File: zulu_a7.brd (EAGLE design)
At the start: 61 x 25.4 mm, 169 parts, among them J1 Pmod 2x6, Q1 12MHz 25ppm (FPGA + FT2232HQ), Q3 MBT3904DW1T1, U1 XC7A35T-1CPG236C, U10 93LC46BT-I/SN, U2 FT2232HQ USB-UART/JTAG Bridge, U3 AS4C32M16SB-6TIN, U4 W25Q128JVSIQ, U8 LTC3569EUDC#TRPBF, X1 Molex 105017-0001 Micro-USB-B

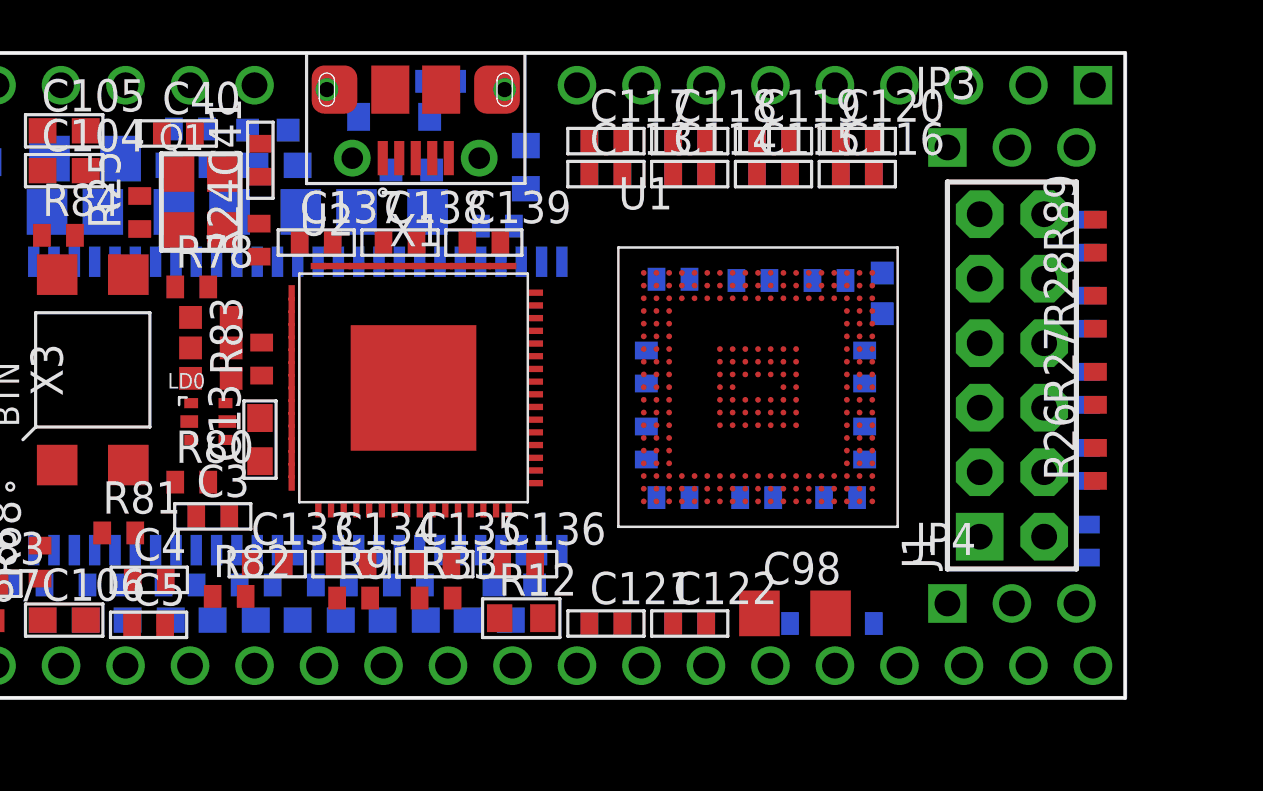
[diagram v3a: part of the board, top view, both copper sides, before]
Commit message: The eight Pmod series resistors go 0402 -> 0201
R26-R33, the 200R in series with the Pmod's eight signal pins. New R0201
package in rcl and an R0201 device on R-US_SMALL; the parts keep their value,
their nets and their 1 % tolerance.

WHAT IT BOUGHT. All eight now sit in a 2x4 block at x 59.49 and 60.09, y 8.60
to 13.99, hard against J1 -- which is where a series resistor for a connector
pin belongs. R33 came off the hand-pin it needed two commits ago: at 0402 it
would not seat within 24 mm of J1 and had to be stranded at x 33; at 0201 the
anchored pass reaches it and it rejoined its seven siblings. Keepout per part
falls 2.95 x 0.97 to 1.75 x 0.37, about a quarter of the area.

THE POWER RATING IS THE THING TO KNOW. These resistors exist for one case: a
Pmod pin driven high into a short. That is 3.3 V across 200 R = 16.5 mA and
54.4 mW, sustained. An 0402 at 1/16 W has 62.5 mW and takes it at 87 %. An 0201
at 1/20 W has 50 mW and is at 109 % -- over rating, not under. It is a fault
case and not normal operation, and Cmod A7 evidently accepts the same, so this
follows that lead. But the margin that existed is gone, and a resistor that
cooks in the fault it was put there to survive is worth knowing about.

The land pattern is marked PROVISIONAL in the package, the way ESP-11 is. It is
0.30 x 0.30 pads on a 0.20 gap, a conventional 0201 land -- deliberately NOT
scaled from R0402 here, which carries a 0.50 mm toe that is generous for hand
work and would pull 0201 parts into tombstones. Check it against the maker's
recommendation and the assembler's 0201 capability before fabricating; 0201 is
not reworkable by hand.

Caught while doing it: the SPEC string "thick film +-1%, 1/16W, 0402" is shared
by 50 parts, so a blind replace relabelled 42 still-0402 resistors as 0201.
Every part's device and SPEC now agree, and the only R-parts without a SPEC are
the six that never had one.

157 placed, 8 real parts parked, unchanged. check_board and validate 0 findings.

Co-Authored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
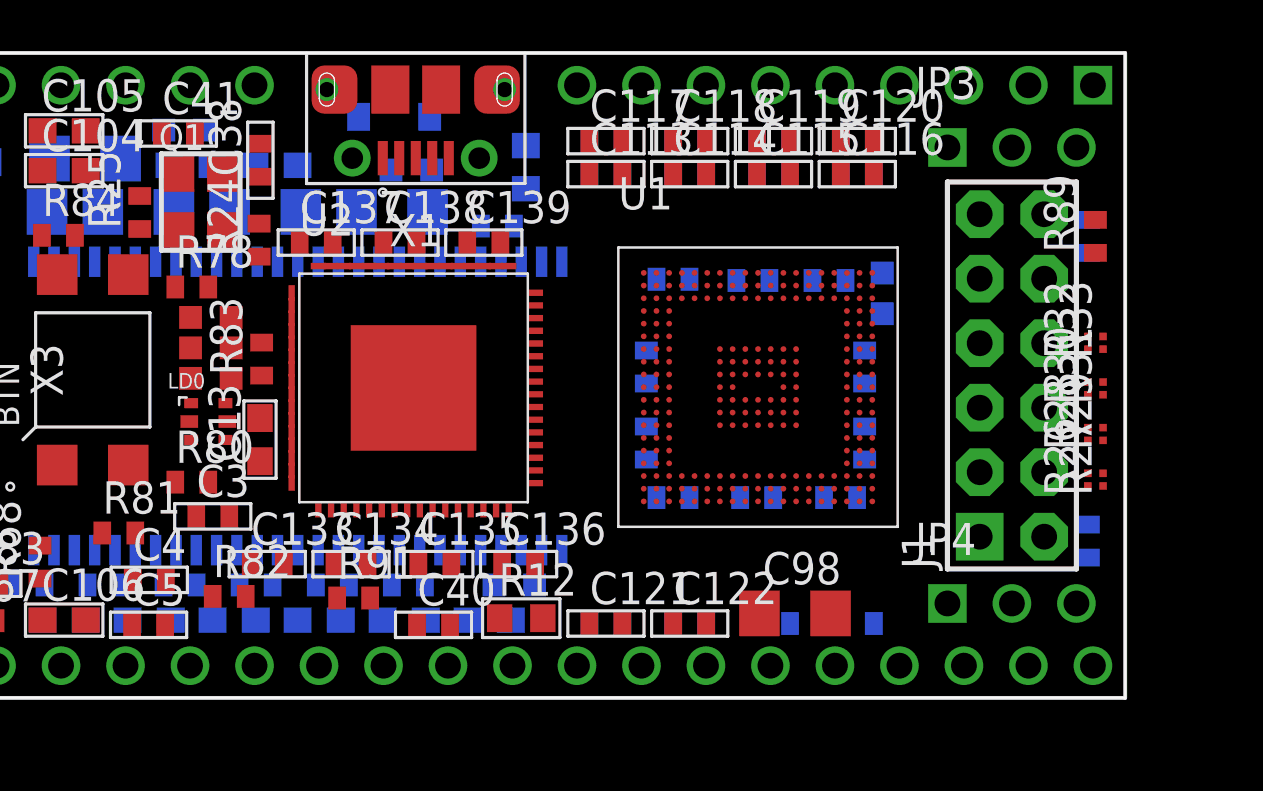
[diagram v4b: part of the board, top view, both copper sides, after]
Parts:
- R26, R27, R28, R29, R30, R31, R32, R33: device rcl:R0402 -> rcl:R0201
- moved R33 28.1 mm to (60.1, 14.0), turned to 90 degrees
- moved R32 27.5 mm to (59.5, 14.0), flipped to the top, turned to 90 degrees
- moved C40 21.8 mm to (33.7, 2.88)
- moved R28 4.81 mm to (59.5, 10.4)
- moved R27 3.61 mm to (60.1, 8.60)
- moved C41 3.40 mm to (23.7, 22.2), turned to 0 degrees
- moved L5 3.30 mm to (23.9, 22.4)
- moved R31 3.06 mm to (60.1, 12.2), flipped to the top
- moved C38 3.02 mm to (26.9, 21.2), flipped to the top, turned to 90 degrees
- moved R29 1.33 mm to (60.1, 10.4), flipped to the top
- moved R26 0.67 mm to (59.5, 8.60)
- flipped R30 to the top
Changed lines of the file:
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@@
 <element name="C137" library="rcl" package="C0402" value="0.1uF" x="29.1" y="17.933"/>
 <element name="C138" library="rcl" package="C0402" value="0.1uF" x="32.4" y="17.933"/>
-<element name="R26" library="rcl" package="R0402" value="200" x="59.79" y="9.198" rot="R90"/>
-<element name="R27" library="rcl" package="R0402" value="200" x="59.79" y="12.194" rot="R90"/>
-<element name="R28" library="rcl" package="R0402" value="200" x="59.79" y="15.19" rot="R90"/>
-<element name="R29" library="rcl" package="R0402" value="200" x="59.5098" y="9.198" rot="MR90"/>
-<element name="R30" library="rcl" package="R0402" value="200" x="59.5098" y="12.194" rot="MR90"/>
-<element name="R31" library="rcl" package="R0402" value="200" x="59.5098" y="15.19" rot="MR90"/>
-<element name="R32" library="rcl" package="R0402" value="200" x="33.998" y="24.284" rot="MR0"/>
-<element name="R33" library="rcl" package="R0402" value="200" x="33.823" y="3.933"/>
+<element name="R26" library="rcl" package="R0201" value="200" x="59.49" y="8.598" rot="R90"/>
+<element name="R27" library="rcl" package="R0201" value="200" x="60.09" y="8.598" rot="R90"/>
+<element name="R28" library="rcl" package="R0201" value="200" x="59.49" y="10.394" rot="R90"/>
+<element name="R29" library="rcl" package="R0201" value="200" x="60.09" y="10.394" rot="R90"/>
+<element name="R30" library="rcl" package="R0201" value="200" x="59.49" y="12.19" rot="R90"/>
+<element name="R31" library="rcl" package="R0201" value="200" x="60.09" y="12.19" rot="R90"/>
+<element name="R32" library="rcl" package="R0201" value="200" x="59.49" y="13.986" rot="R90"/>
+<element name="R33" library="rcl" package="R0201" value="200" x="60.09" y="13.986" rot="R90"/>
 <element name="U$2" library="ctambe" package="CC_CC" value="" x="5.0585" y="-6.4415"/>
 <element name="U$3" library="ctambe" package="CC_BY" value="" x="10.895" y="-7.722"/>
@@
 <element name="L3" library="ctambe" package="IND2520" value="2.2uH" x="12.45" y="16.34" rot="MR0"/>
 <element name="L4" library="ctambe" package="IND0603" value="FB 600R@100MHz" x="32.845" y="20.79" rot="MR0"/>
-<element name="L5" library="ctambe" package="IND0603" value="FB 600R@100MHz" x="27.196" y="22.36" rot="MR0"/>
+<element name="L5" library="ctambe" package="IND0603" value="FB 600R@100MHz" x="23.896" y="22.36" rot="MR0"/>
 <element name="L6" library="ctambe" package="IND0603" value="FB 600R@100MHz" x="51.392" y="15.932" rot="MR90"/>
 <element name="L7" library="ctambe" package="IND0603" value="FB 600R@100MHz" x="36.9" y="4.45" rot="MR0"/>
@@
 <element name="C139" library="rcl" package="C0402" value="3.3uF" x="35.7" y="17.933"/>
 <element name="C39" library="rcl" package="C0402" value="3.3uF" x="36.234" y="18.58" rot="MR0"/>
-<element name="C40" library="rcl" package="C0402" value="100nF" x="23.6705" y="22.23"/>
-<element name="C41" library="rcl" package="C0402" value="100nF" x="26.9" y="21.176" rot="R90"/>
+<element name="C40" library="rcl" package="C0402" value="100nF" x="33.721" y="2.878"/>
+<element name="C41" library="rcl" package="C0402" value="100nF" x="23.6705" y="22.23"/>
 <element name="R71" library="rcl" package="R0402" value="180K 1%" x="6.169" y="2.828" rot="MR0"/>
 <element name="C83" library="rcl" package="C0402" value="20pF" x="15.973" y="4.5"/>
@@
 <element name="R85" library="rcl" package="R0402" value="10K" x="15.65" y="13.364" rot="MR90"/>
 <element name="R86" library="rcl" package="R0402" value="10K" x="15.65" y="16.36" rot="MR90"/>
-<element name="R89" library="rcl" package="R0402" value="10K" x="59.79" y="18.186" rot="R90"/>
+<element name="R89" library="rcl" package="R0402" value="10K" x="59.79" y="18.178" rot="R90"/>
 <element name="R90" library="rcl" package="R0402" value="10K" x="59.5098" y="6.176" rot="MR90"/>
 <element name="R91" library="rcl" package="R0402" value="10K" x="30.573" y="3.933"/>
-<element name="R92" library="rcl" package="R0402" value="10K" x="59.5098" y="18.186" rot="MR90"/>
+<element name="R92" library="rcl" package="R0402" value="10K" x="59.5098" y="18.178" rot="MR90"/>
 <element name="R93" library="rcl" package="R0402" value="10K" x="42.1" y="13.034" rot="MR90"/>
 <element name="R94" library="rcl" package="R0402" value="10K" x="50.7" y="13.034" rot="MR90"/>
@@
 <element name="BTN" library="ctambe" package="PTA-142" value="PTA-142" x="20.3" y="12.92" rot="R90"/>
 <element name="Q1" library="ctambe" package="32X25" value="12MHz 25ppm (FPGA + FT2232HQ)" x="23.7" y="20.63"/>
-<element name="C38" library="rcl" package="C0402" value="0.01uF" x="24.146" y="22.41" rot="MR0"/>
+<element name="C38" library="rcl" package="C0402" value="0.01uF" x="26.9" y="21.176" rot="R90"/>
 <element name="J1" library="ctambe" package="2X06" value="Pmod 2x6" x="56.5" y="12.7" rot="R90"/>
 <element name="R24" library="rcl" package="R0402" value="33" x="26.85" y="18.028" rot="R90"/>

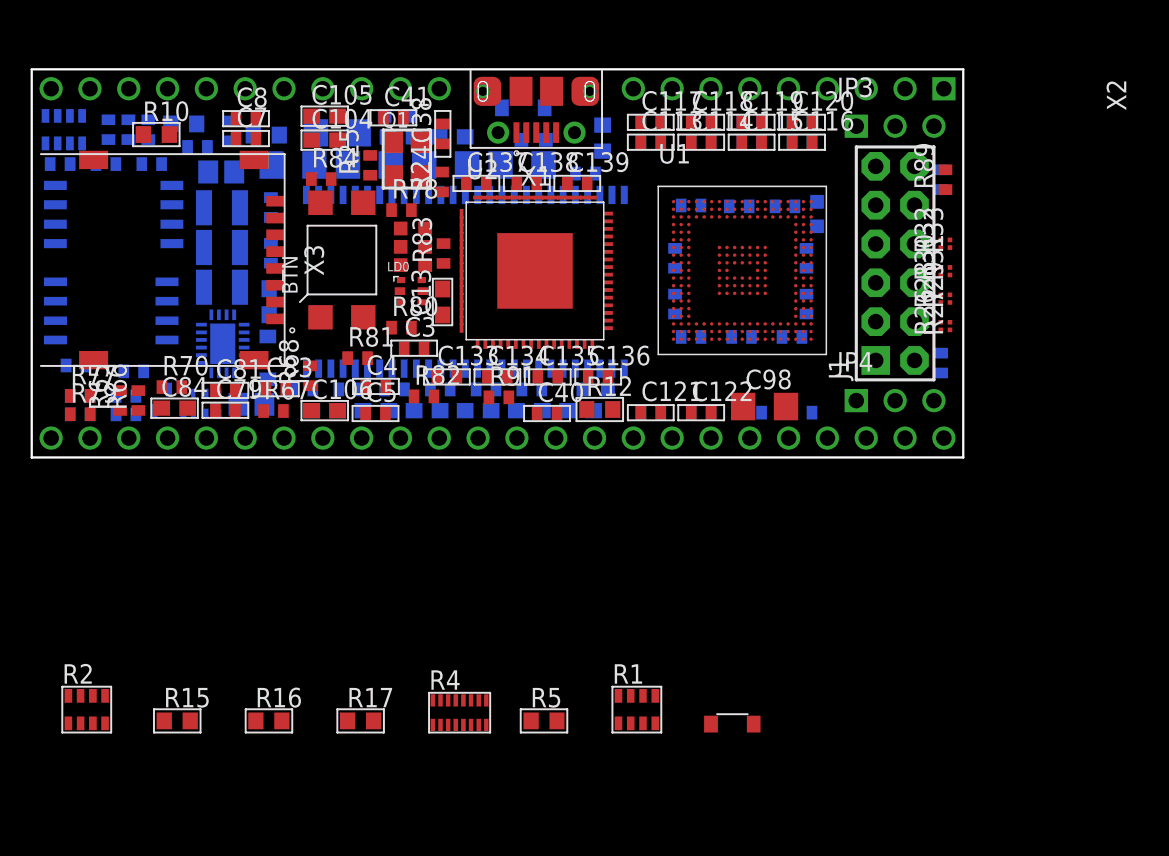
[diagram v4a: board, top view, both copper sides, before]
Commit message: The eight XADC resistors go 0603 -> 0201, and five parts come off the park
R10-R17, both XADC channels: the 2.32k/1k divider, the 140R into AIN_P and the
845R from AIN_N to ground. R-US_ gains an R0201 device; values, nets and 1 %
tolerance unchanged.

POWER IS NOT THE QUESTION HERE, unlike the Pmod eight. The only ones carrying
current are R10/R14 at the top of a 3.32k divider: 2.3 mW at a 3.3 V input,
5.3 mW at 5 V, against an 0201's 50 mW. Eleven per cent of rating at the worst
case, nine times the margin. R12/R13/R16/R17 sit on XADC inputs and carry
leakage. Nothing here cooks the way a shorted Pmod pin does.

Nor does size touch what this circuit depends on. R13 = 845R is matching
R12 + (R10||R11) = 838.8R so both XADC inputs see the same source impedance,
and that is a tolerance property. 1 % is 1 % at any size.

WHAT IT FREED. Parked real parts 8 -> 3. R15, R16 and R17 seated, and the space
released also let D3 and R5 in. The four that matter most are close: R12 5.6 mm
from the ball centre, R17 5.5, R16 6.2, R13 7.2 -- the network at the XADC pins
is tight to the package. R10/R11 and R14/R15 landed 20 to 24 mm out, which is
fine for a divider that only scales the input before it reaches that network.

WHAT IS LEFT: R1, R2 and R4, all three array packages, which no amount of chip
shrinking helps. Splitting them into 16 discrete 0402 is still the open option.

AND ONE THING TO LOOK AT. D3 is on the board now, at 51.3 mm from X2 pad 1. I
had left it parked on purpose because 55 mm from the pin a TVS protects is not
protection. Freeing space did not fix that -- it just let the anchored pass seat
it, at the far end, where it clamps no better than it did unplaced. It now looks
placed. It is not placed usefully, and dropping JP3/JP4 is still what would give
it the corner it wants.

161 placed. check_board and validate 0 findings.

Co-Authored-By: Claude Opus 5 <noreply@anthropic.com>
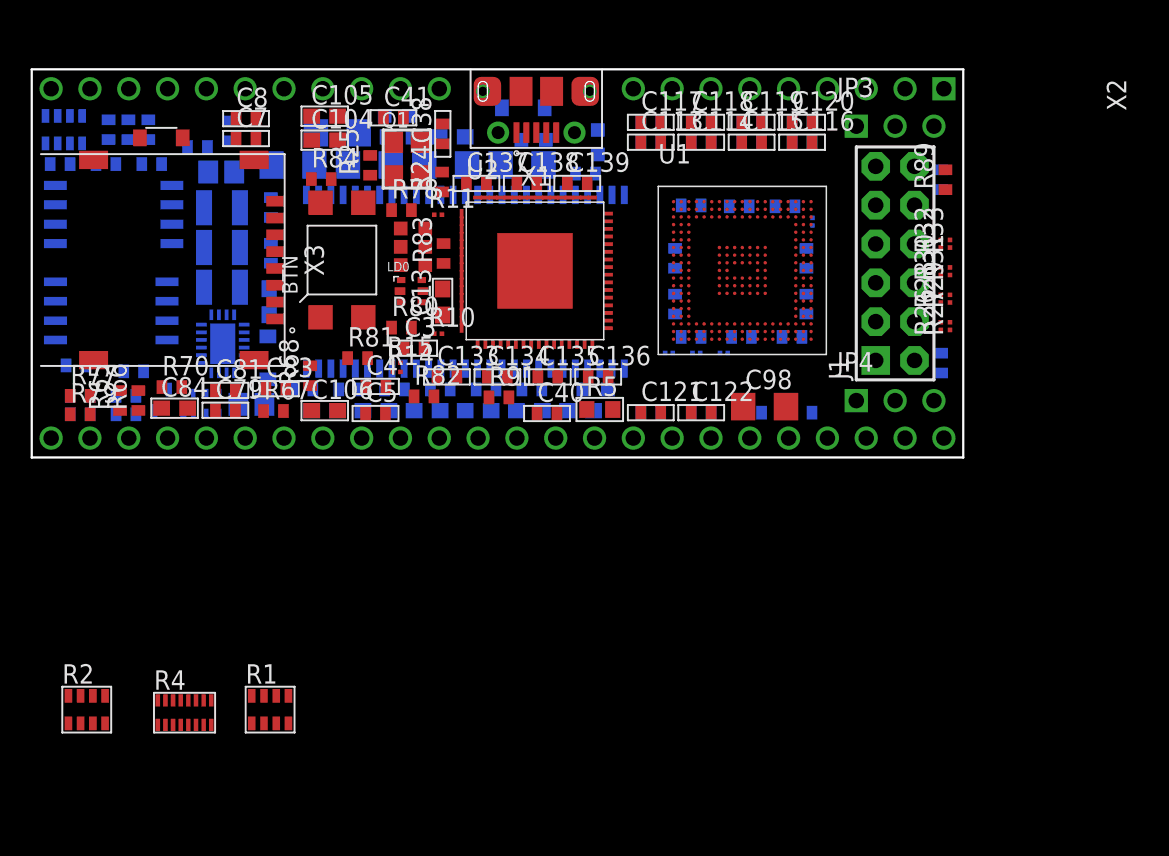
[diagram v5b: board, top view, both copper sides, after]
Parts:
- R10, R11, R12, R13, R14, R15, R16, R17: device rcl:R0603 -> rcl:R0201
- moved D3 53.6 mm to (8.48, 20.9)
- moved R16 36.9 mm to (43.5, 6.84), flipped to the bottom
- moved R17 33.8 mm to (45.3, 6.84), flipped to the bottom
- moved R15 27.5 mm to (23.9, 6.20)
- moved R1 24.0 mm to (14.8, -16.5)
- moved R10 22.6 mm to (26.6, 8.10)
- moved R14 21.4 mm to (23.9, 5.60), flipped to the top
- moved R5 20.7 mm to (37.2, 3.14)
- moved R12 18.6 mm to (51.1, 15.4), flipped to the bottom, turned to 90 degrees
- moved L6 18.5 mm to (36.9, 4.45), turned to 0 degrees
- moved R4 18.0 mm to (10.0, -16.7)
- moved L7 16.2 mm to (37.0, 20.6), turned to 90 degrees
- moved R13 14.7 mm to (41.7, 6.84), turned to 0 degrees
- moved R11 12.4 mm to (26.6, 15.9), flipped to the top
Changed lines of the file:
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@@
 <element name="R2" library="ctambe" package="742C083" value="4.7K" x="2.8" y="-16.5"/>
 <element name="U1" library="ctambe" package="XC7A35T-CPG236" value="XC7A35T-1CPG236C" x="42" y="16.74"/>
-<element name="R10" library="rcl" package="R0603" value="2.32K" x="8.154" y="21.132"/>
-<element name="R11" library="rcl" package="R0603" value="1K" x="15.349" y="21.102" rot="MR0"/>
-<element name="R12" library="rcl" package="R0603" value="140" x="37.174" y="3.14"/>
-<element name="R13" library="rcl" package="R0603" value="845" x="37.357" y="20.904" rot="MR90"/>
-<element name="R14" library="rcl" package="R0603" value="2.32K" x="9.949" y="21.83" rot="MR0"/>
-<element name="R15" library="rcl" package="R0603" value="1K" x="9.524" y="-17.238"/>
-<element name="R16" library="rcl" package="R0603" value="140" x="15.524" y="-17.238"/>
-<element name="R17" library="rcl" package="R0603" value="845" x="21.524" y="-17.238"/>
+<element name="R10" library="rcl" package="R0201" value="2.32K" x="26.594" y="8.1"/>
+<element name="R11" library="rcl" package="R0201" value="1K" x="26.594" y="15.885"/>
+<element name="R12" library="rcl" package="R0201" value="140" x="51.092" y="15.43" rot="MR90"/>
+<element name="R13" library="rcl" package="R0201" value="845" x="41.698" y="6.84" rot="MR0"/>
+<element name="R14" library="rcl" package="R0201" value="2.32K" x="23.878" y="5.6"/>
+<element name="R15" library="rcl" package="R0201" value="1K" x="23.878" y="6.2"/>
+<element name="R16" library="rcl" package="R0201" value="140" x="43.494" y="6.84" rot="MR0"/>
+<element name="R17" library="rcl" package="R0201" value="845" x="45.29" y="6.84" rot="MR0"/>
 <element name="C3" library="rcl" package="C0402" value="0.1uF" x="25.025" y="7.15"/>
 <element name="C4" library="rcl" package="C0402" value="0.1uF" x="22.525" y="4.65"/>
@@
 <element name="JP3" library="pinhead" package="1X03-NOSILK" value="JTAG TCK/TMS/GND" x="56.5" y="21.68"/>
 <element name="JP4" library="pinhead" package="1X03-NOSILK" value="JTAG TDI/TDO/3V3" x="56.5" y="3.72"/>
-<element name="R4" library="ctambe" package="741X163" value="100" x="28" y="-16.7"/>
-<element name="R5" library="rcl" package="R0603" value="5.1K" x="33.524" y="-17.238"/>
-<element name="R1" library="ctambe" package="742C083" value="4.7K" x="38.8" y="-16.5"/>
+<element name="R4" library="ctambe" package="741X163" value="100" x="10" y="-16.7"/>
+<element name="R5" library="rcl" package="R0603" value="5.1K" x="37.174" y="3.14"/>
+<element name="R1" library="ctambe" package="742C083" value="4.7K" x="14.8" y="-16.5"/>
 <element name="U8" library="ctambe" package="LTC3569-QFN20" value="LTC3569EUDC#TRPBF" x="12.5" y="7.44" rot="MR0"/>
 <element name="D1" library="ctambe" package="SOD123" value="PMEG2020EJ,115" x="15.45" y="6.518" rot="MR90"/>
 <element name="D2" library="ctambe" package="SOD123" value="PMEG2020EJ,115" x="32.17" y="22.884" rot="MR0"/>
-<element name="D3" library="ctambe" package="SOD123" value="SMF5.0A" x="45.85" y="-17.45"/>
+<element name="D3" library="ctambe" package="SOD123" value="SMF5.0A" x="8.48" y="20.92"/>
 <element name="C78" library="rcl" package="C0805" value="22uF 10V" x="12.401" y="18.679" rot="MR0"/>
 <element name="R67" library="rcl" package="R0402" value="3.48K 1%" x="15.821" y="3.04"/>
@@
 <element name="L4" library="ctambe" package="IND0603" value="FB 600R@100MHz" x="32.845" y="20.79" rot="MR0"/>
 <element name="L5" library="ctambe" package="IND0603" value="FB 600R@100MHz" x="23.896" y="22.36" rot="MR0"/>
-<element name="L6" library="ctambe" package="IND0603" value="FB 600R@100MHz" x="51.392" y="15.932" rot="MR90"/>
-<element name="L7" library="ctambe" package="IND0603" value="FB 600R@100MHz" x="36.9" y="4.45" rot="MR0"/>
+<element name="L6" library="ctambe" package="IND0603" value="FB 600R@100MHz" x="36.9" y="4.45" rot="MR0"/>
+<element name="L7" library="ctambe" package="IND0603" value="FB 600R@100MHz" x="37.045" y="20.63" rot="MR90"/>
 <element name="C123" library="rcl" package="C0402" value="100nF" x="49.75" y="7.89" rot="MR0"/>
 <element name="C124" library="rcl" package="C0402" value="470nF" x="43.15" y="16.49" rot="MR0"/>
